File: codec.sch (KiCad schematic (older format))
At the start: 10 parts, among them U4 WM8731SEDS

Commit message: "0.1u" -> "100n"; use 1206 10u for bulk decoupling
The 1206 size has a much better derating-vs-bias-voltage curve.
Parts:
- C21, C22, C23, C24: value 0.1u -> 100n
- C29, C30, C31, C32: footprint Capacitor_SMD:C_0603_1608Metric -> Capacitor_SMD:C_1206_3216Metric
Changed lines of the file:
@@
 P 2100 2900
 F 0 "C21" H 2215 2946 50  0000 L CNN
-F 1 "0.1u" H 2215 2855 50  0000 L CNN
+F 1 "100n" H 2215 2855 50  0000 L CNN
 F 2 "Capacitor_SMD:C_0603_1608Metric" H 2138 2750 50  0001 C CNN
 F 3 "~" H 2100 2900 50  0001 C CNN
@@
 F 0 "C29" H 2665 2946 50  0000 L CNN
 F 1 "10u" H 2665 2855 50  0000 L CNN
-F 2 "Capacitor_SMD:C_0603_1608Metric" H 2588 2750 50  0001 C CNN
+F 2 "Capacitor_SMD:C_1206_3216Metric" H 2588 2750 50  0001 C CNN
 F 3 "~" H 2550 2900 50  0001 C CNN
 	1    2550 2900
@@
 P 2100 3800
 F 0 "C22" H 2215 3846 50  0000 L CNN
-F 1 "0.1u" H 2215 3755 50  0000 L CNN
+F 1 "100n" H 2215 3755 50  0000 L CNN
 F 2 "Capacitor_SMD:C_0603_1608Metric" H 2138 3650 50  0001 C CNN
 F 3 "~" H 2100 3800 50  0001 C CNN
@@
 F 0 "C30" H 2665 3846 50  0000 L CNN
 F 1 "10u" H 2665 3755 50  0000 L CNN
-F 2 "Capacitor_SMD:C_0603_1608Metric" H 2588 3650 50  0001 C CNN
+F 2 "Capacitor_SMD:C_1206_3216Metric" H 2588 3650 50  0001 C CNN
 F 3 "~" H 2550 3800 50  0001 C CNN
 	1    2550 3800
@@
 P 2100 4700
 F 0 "C23" H 2215 4746 50  0000 L CNN
-F 1 "0.1u" H 2215 4655 50  0000 L CNN
+F 1 "100n" H 2215 4655 50  0000 L CNN
 F 2 "Capacitor_SMD:C_0603_1608Metric" H 2138 4550 50  0001 C CNN
 F 3 "~" H 2100 4700 50  0001 C CNN
@@
 F 0 "C31" H 2665 4746 50  0000 L CNN
 F 1 "10u" H 2665 4655 50  0000 L CNN
-F 2 "Capacitor_SMD:C_0603_1608Metric" H 2588 4550 50  0001 C CNN
+F 2 "Capacitor_SMD:C_1206_3216Metric" H 2588 4550 50  0001 C CNN
 F 3 "~" H 2550 4700 50  0001 C CNN
 	1    2550 4700
@@
 P 2100 5600
 F 0 "C24" H 2215 5646 50  0000 L CNN
-F 1 "0.1u" H 2215 5555 50  0000 L CNN
+F 1 "100n" H 2215 5555 50  0000 L CNN
 F 2 "Capacitor_SMD:C_0603_1608Metric" H 2138 5450 50  0001 C CNN
 F 3 "~" H 2100 5600 50  0001 C CNN
@@
 F 0 "C32" H 2665 5646 50  0000 L CNN
 F 1 "10u" H 2665 5555 50  0000 L CNN
-F 2 "Capacitor_SMD:C_0603_1608Metric" H 2588 5450 50  0001 C CNN
+F 2 "Capacitor_SMD:C_1206_3216Metric" H 2588 5450 50  0001 C CNN
 F 3 "~" H 2550 5600 50  0001 C CNN
 	1    2550 5600

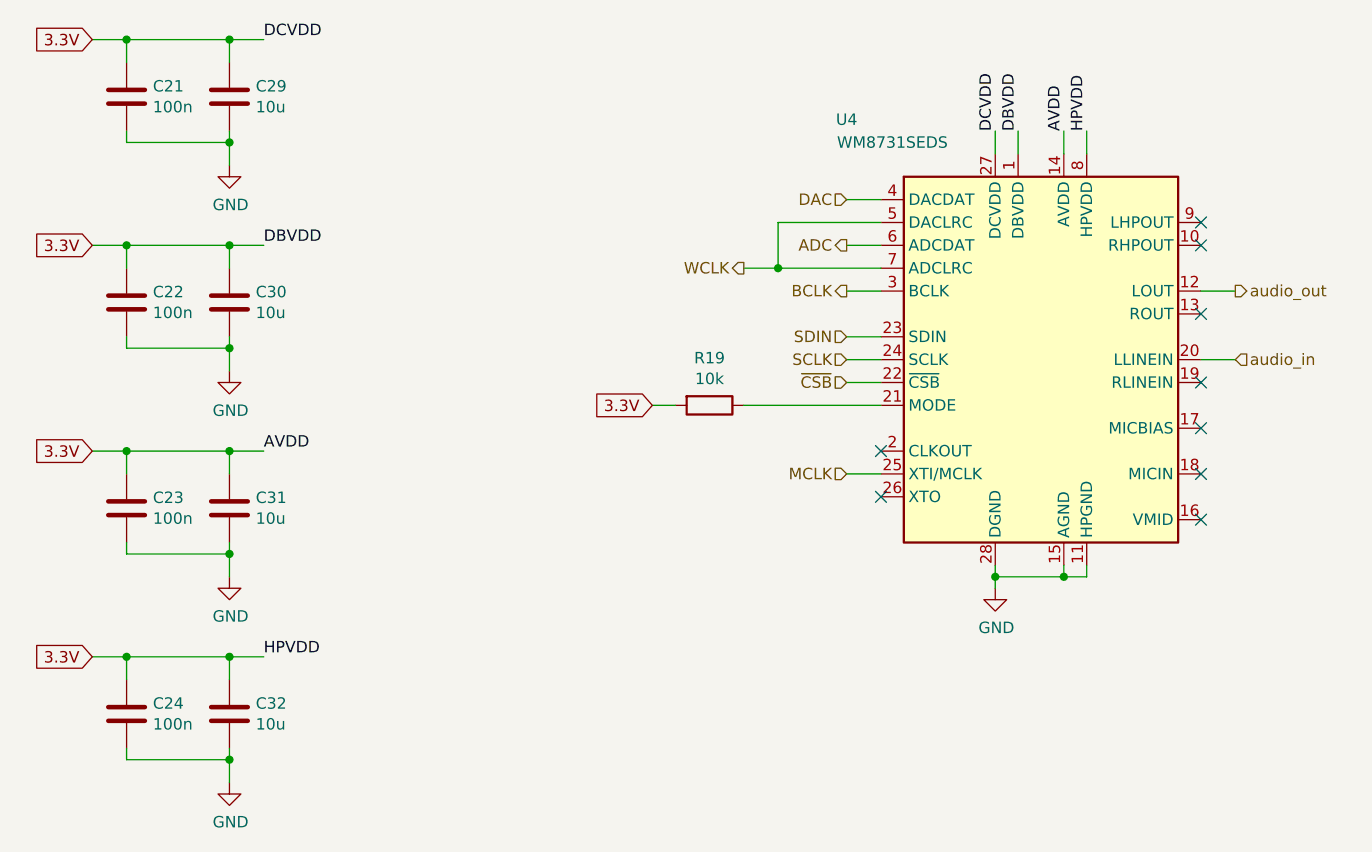
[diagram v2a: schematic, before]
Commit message: Use actual parts from Mouser order
I was able to order the ATSAME51J20A-AU and the WM8731CLSEFL.
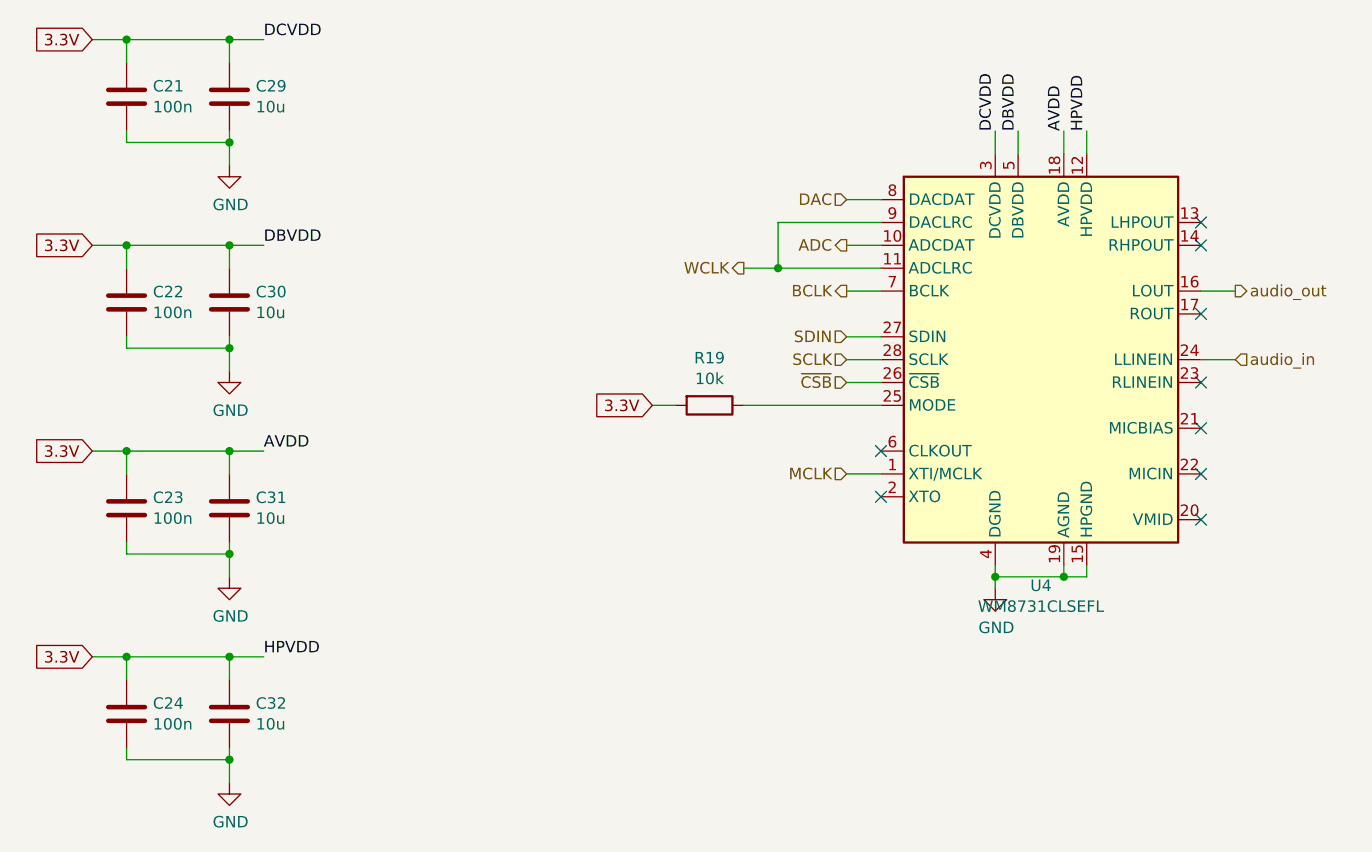
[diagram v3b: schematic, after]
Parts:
- removed U4: WM8731SEDS, Package_SO:SSOP-28_5.3x10.2mm_P0.65mm, symbol Audio:WM8731SEDS
- added U4: WM8731CLSEFL, Package_DFN_QFN:QFN-28-1EP_5x5mm_P0.5mm_EP3.35x3.35mm, symbol Audio:WM8731CLSEFL
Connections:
- net 3.3V: now also U4.12 (HPVDD), U4.18 (AVDD), U4.3 (DCVDD), U4.5 (DBVDD)
- net ADC: now also U4.10 (ADCDAT)
- net BCLK: now also U4.7 (BCLK)
- net DAC: now also U4.8 (DACDAT)
- net GND: now also U4.15 (HPGND), U4.19 (AGND), U4.29 (AGND), U4.4 (DGND)
- net MCLK: now also U4.1 (XTI/MCLK)
- net SCLK: now also U4.28 (SCLK)
- net SDIN: now also U4.27 (SDIN)
- net WCLK: now also U4.11 (ADCLRC), U4.9 (DACLRC)
- net audio_in: now also U4.24 (LLINEIN)
- net audio_out: now also U4.16 (LOUT)
- net ~CSB: now also U4.26 (~CSB)
- net at R19.1: now also U4.25 (MODE)
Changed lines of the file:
@@
 $EndDescr
-$Comp
-L Audio:WM8731SEDS U4
-U 1 1 6005E3AC
-P 6100 4050
-F 0 "U4" H 5250 5100 50  0000 C CNN
-F 1 "WM8731SEDS" H 5450 5000 50  0000 C CNN
-F 2 "Package_SO:SSOP-28_5.3x10.2mm_P0.65mm" H 6100 2750 50  0001 C CNN
-F 3 "https://statics.cirrus.com/pubs/proDatasheet/WM8731_v4.9.pdf" H 6100 4050 50  0001 C CNN
-	1    6100 4050
-	1    0    0    -1
-$EndComp
 $Comp
 L power:GND #PWR044
@@
 Connection ~ 2550 5350
 Connection ~ 2100 5350
+$Comp
+L Audio:WM8731CLSEFL U4
+U 1 1 6087E599
+P 6100 4050
+F 0 "U4" H 6100 3061 50  0000 C CNN
+F 1 "WM8731CLSEFL" H 6100 2970 50  0000 C CNN
+F 2 "Package_DFN_QFN:QFN-28-1EP_5x5mm_P0.5mm_EP3.35x3.35mm" H 6100 2750 50  0001 C CNN
+F 3 "https://statics.cirrus.com/pubs/proDatasheet/WM8731_v4.9.pdf" H 6100 4050 50  0001 C CNN
+	1    6100 4050
+	1    0    0    -1
+$EndComp
 $EndSCHEMATC
